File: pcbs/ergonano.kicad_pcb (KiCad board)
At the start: 2 copper layers, 171.6 x 164.6 mm, 87 parts

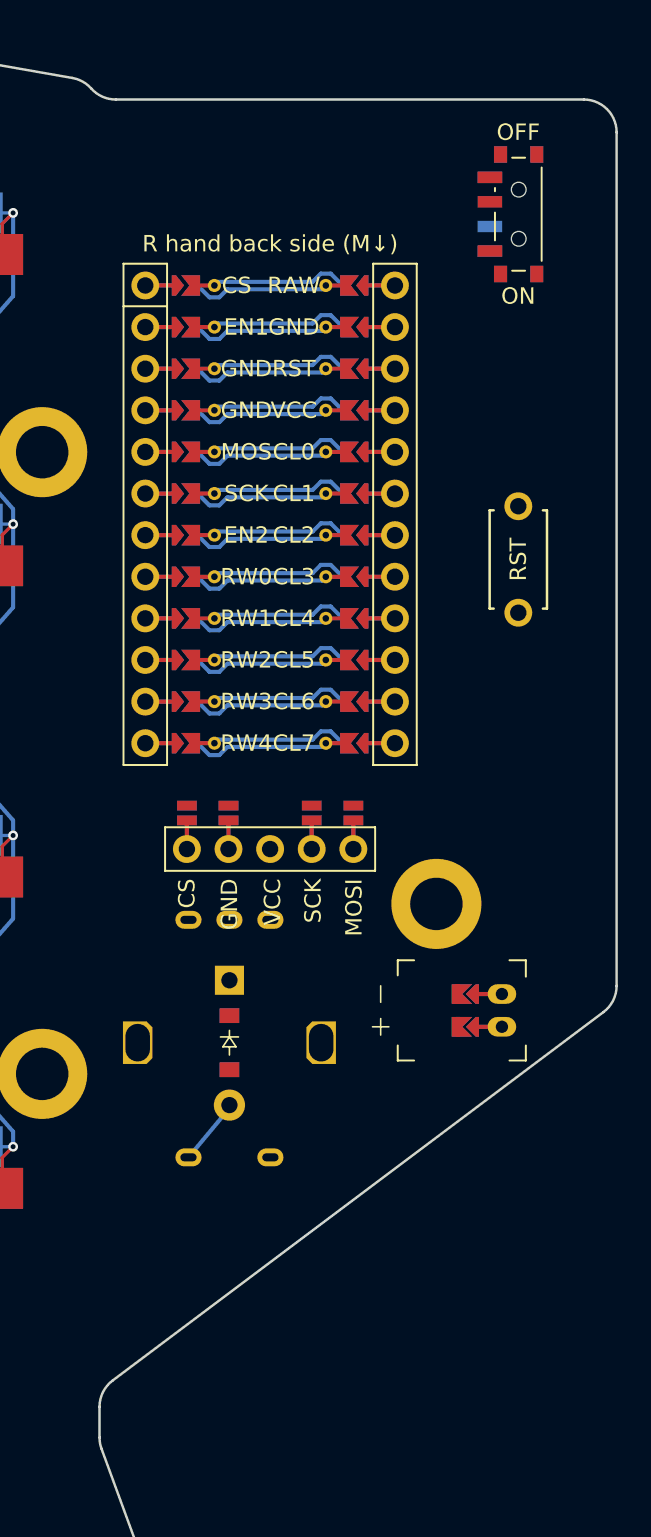
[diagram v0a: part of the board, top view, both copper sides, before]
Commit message: Tweaked layout, moved battery connector
shrinks the overall PCB by shrinking the mcu_padding
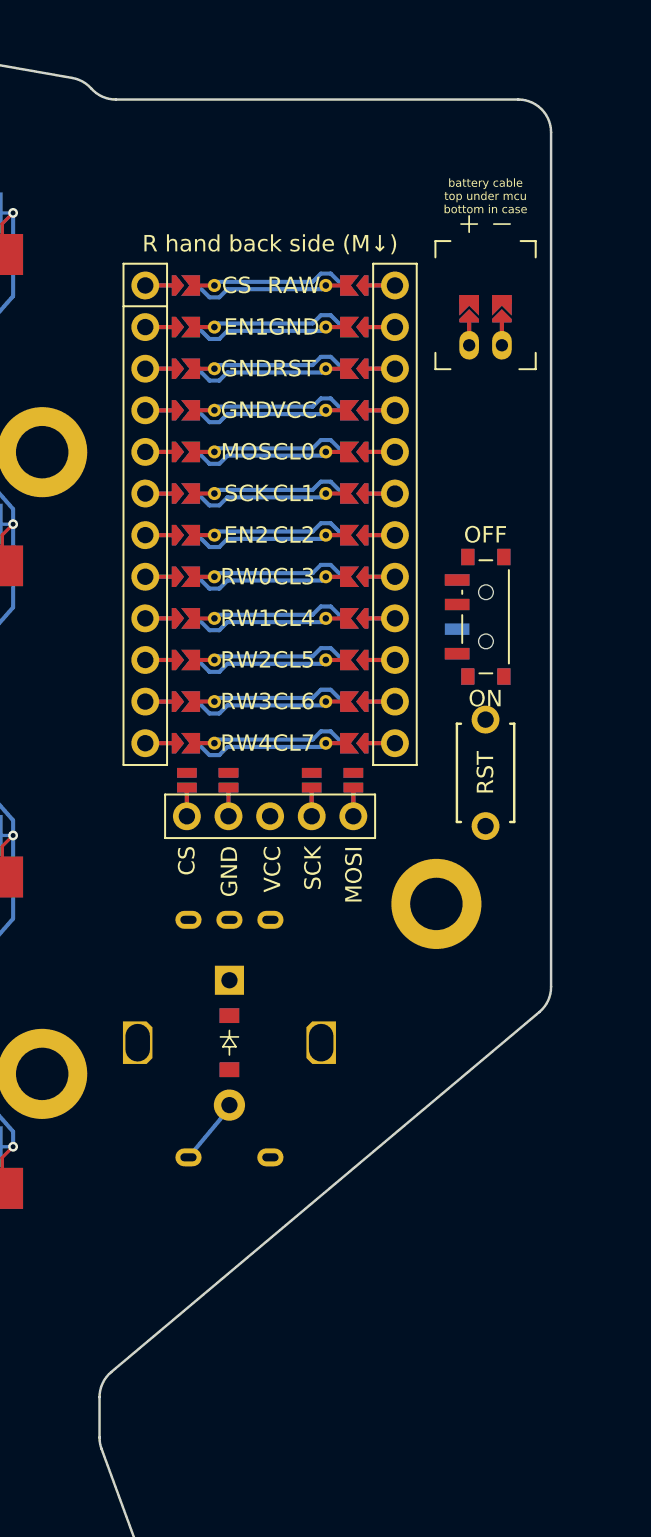
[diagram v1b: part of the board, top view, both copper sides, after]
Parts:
- moved JST1 40.6 mm to (200.6, 52.0), turned to 180 degrees
- moved PWR1 24.7 mm to (200.6, 68.6)
- moved RST1 13.2 mm to (200.6, 78.1)
- moved DISP1 2.00 mm to (187.4, 64.0)
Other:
- board size 171.6 x 164.6 mm -> 167.6 x 164.6 mm
- board text added: "battery cable top under mcu bottom in case"

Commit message: Use a drill for all screw holes on generated pcb plates
don't plate the encoder mounting holes (kicad jlcpcb violation)
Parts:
- added D35: , ceoloide:diode_tht_sod123, F.Cu at (139.2, 159.1)
- added D36: , ceoloide:diode_tht_sod123, F.Cu at (153.7, 146.9)
- added D37: , ceoloide:diode_tht_sod123, F.Cu at (151.4, 173.7)
- added D38: , ceoloide:diode_tht_sod123, F.Cu at (166.0, 161.5)
- added D39: , ceoloide:diode_tht_sod123, F.Cu at (185.0, 94.6)
- moved D34 67.0 mm to (134.2, 138.4), turned to 40 degrees
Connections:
- D34 pad 1: RW4 -> RW0
- D34 pad 2: encoder_encoder -> t_col0_near
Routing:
- net RW0: track 0.00 -> 34.6 mm
- net RW3: track 0.00 -> 34.6 mm
- net RW2: track 0.00 -> 34.6 mm
- net RW1: track 0.00 -> 34.6 mm
- net RW4: track 0.00 -> 25.9 mm
- net ring_num: track 13.8 -> 18.1 mm
- net middle_top: track 13.8 -> 18.1 mm
- net middle_num: track 13.8 -> 18.1 mm
- net index_num: track 13.8 -> 18.1 mm
- net pinky_num: track 13.8 -> 18.1 mm
- net outer_num: track 13.8 -> 18.1 mm
- net innermod_num: track 13.8 -> 18.1 mm
- net inner_num: track 13.8 -> 18.1 mm
- net ring_top: track 13.8 -> 18.1 mm
- net index_top: track 13.8 -> 18.1 mm
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
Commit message: moved the battery connector text
also resized to meet JLCPCB minimums
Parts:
- moved PWR1 9.52 mm to (200.6, 59.0)
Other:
- board text added: "mount battery connector top side if under mcu bottom side if larger"
- board text removed: "battery cable top under mcu bottom in case"
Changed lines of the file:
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@@
   (footprint "ceoloide:power_switch_smd_side"
     (layer "F.Cu")
-    (at 200.5875 68.57499999999999 0)
+    (at 200.5875 59.05 0)
     (property "Reference" "PWR1"
       (at -3.6 0 -90)
@@
     )
   )
-  (gr_text "battery cable\ntop under mcu\nbottom in case"
-    (at 200.5875 42.9 0)
-    (layer "F.SilkS" )
-    (effects
-      (font
-        (size 0.5 0.5)
-        (thickness 0.15)
-      )
-    )
-  )
-  (gr_text "battery cable\ntop under mcu\nbottom in case"
-    (at 200.5875 42.9 0)
-    (layer "B.SilkS" )
-    (effects
-      (font
-        (size 0.5 0.5)
-        (thickness 0.15)
-      )
+  (gr_text "mount battery connector\ntop side if under mcu\nbottom side if larger"
+    (at 187.4375 40 0)
+    (layer "F.SilkS" )
+    (effects
+      (font
+        (size 1 1)
+        (thickness 0.15)
+      )
+    )
+  )
+  (gr_text "mount battery connector\ntop side if under mcu\nbottom side if larger"
+    (at 187.4375 40 0)
+    (layer "B.SilkS" )
+    (effects
+      (font
+        (size 1 1)
+        (thickness 0.15)
+      )

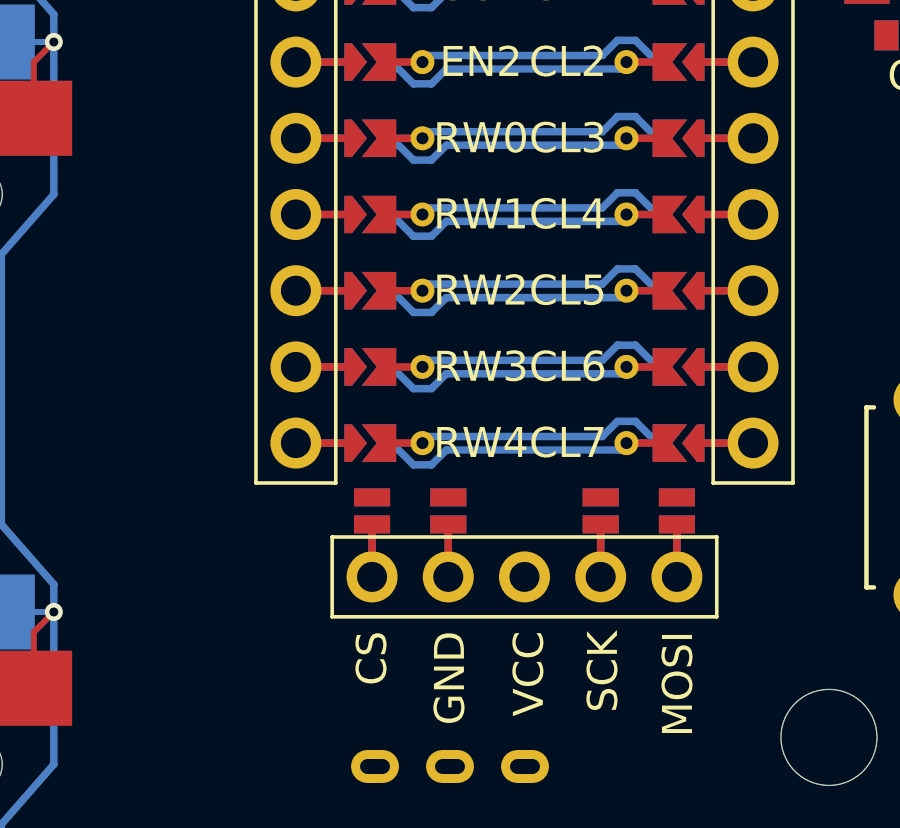
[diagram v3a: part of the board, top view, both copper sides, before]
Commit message: Small renames, tweaks to freerouting rules
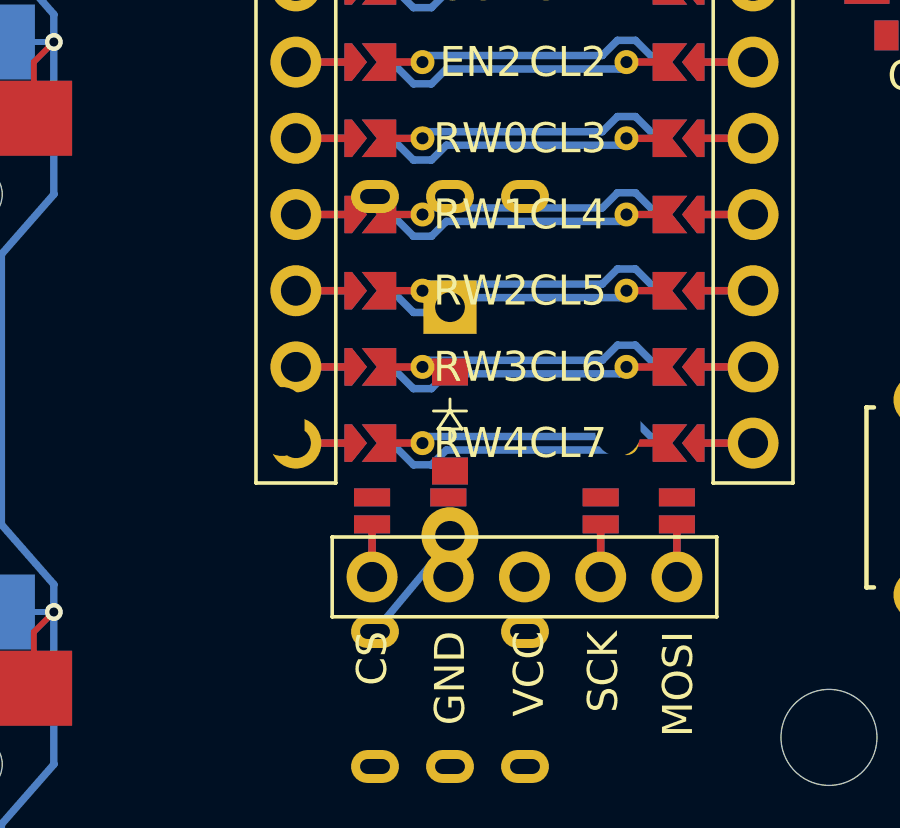
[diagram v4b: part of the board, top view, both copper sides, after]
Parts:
- added D40: , ceoloide:diode_tht_sod123, F.Cu at (185.0, 75.6)
- added RE2: , ceoloide:rotary_encoder_ec11_ec12, F.Cu at (185.0, 75.6)
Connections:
- net encoder_encoder renamed encoder_mcu
- D39 pad 1: RW4 -> (no net)
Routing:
- net (no net): track 918.1 -> 922.0 mm
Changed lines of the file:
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@@
   (title_block
     (title "ergonano")
-    (date "2026-10-30")
+    (date "2026-10-31")
     (rev "0.1")
     (company "aevumdecessus")
@@
 (net 96 "JST1_1")
 (net 97 "JST1_2")
-(net 98 "encoder_encoder")
+(net 98 "encoder_mcu")
+(net 99 "encoder_encoder")
   (footprint "ceoloide:switch_mx"
     (layer "B.Cu")
@@
     (pad "C" thru_hole oval (at -2.5 7.5 180) (size 1.6 1.1) (drill oval 1 0.5) (layers "*.Cu" "*.Mask") (net 62 "EN2"))
     (pad "S1" thru_hole oval (at -2.5 -7 180) (size 1.6 1.1) (drill oval 1 0.5) (layers "*.Cu" "*.Mask") (net 39 "CL6"))
-    (pad "S2" thru_hole oval (at 2.5 -7 180) (size 1.6 1.1) (drill oval 1 0.5) (layers "*.Cu" "*.Mask") (net 98 "encoder_encoder"))
+    (pad "S2" thru_hole oval (at 2.5 -7 180) (size 1.6 1.1) (drill oval 1 0.5) (layers "*.Cu" "*.Mask") (net 98 "encoder_mcu"))
+    (pad "" np_thru_hole oval
+      (at -5.6 0 90)
+      (size 2.3 1.5)
+      (drill oval 2.3 1.5)
+      (layers "*.Cu" "*.Mask")
+    )
+    (pad "" np_thru_hole oval
+      (at 5.6 0 90)
+      (size 2.3 1.5)
+      (drill oval 2.3 1.5)
+      (layers "*.Cu" "*.Mask")
+    )
+    (fp_rect (start -5.9 -6) (end 5.9 6) (layer "Dwgs.User") (stroke (width 0.15) (type solid)) (fill none))
+  )
+  (footprint "ceoloide:rotary_encoder_ec11_ec12"
+    (layer "F.Cu")
+    (at 184.95499999999998 75.57 180)
+    (property "Reference" "RE2"
+      (at 0 -8.5)
+      (layer "F.SilkS")
+      hide
+      (effects (font (size 1 1) (thickness 0.15)))
+    )
+    (attr through_hole)
+    (pad "A" thru_hole oval (at 2.5 7.5 180) (size 1.6 1.1) (drill oval 1 0.5) (layers "*.Cu" "*.Mask") (net 59 "EN1"))
+    (pad "B" thru_hole oval (at 0 7.5 180) (size 1.6 1.1) (drill oval 1 0.5) (layers "*.Cu" "*.Mask") (net 3 "GND"))
+    (pad "C" thru_hole oval (at -2.5 7.5 180) (size 1.6 1.1) (drill oval 1 0.5) (layers "*.Cu" "*.Mask") (net 62 "EN2"))
+    (pad "S1" thru_hole oval (at -2.5 -7 180) (size 1.6 1.1) (drill oval 1 0.5) (layers "*.Cu" "*.Mask") (net 39 "CL6"))
+    (pad "S2" thru_hole oval (at 2.5 -7 180) (size 1.6 1.1) (drill oval 1 0.5) (layers "*.Cu" "*.Mask") (net 99 "encoder_encoder"))
     (pad "" np_thru_hole oval
       (at -5.6 0 90)
@@
       (fp_line (start -0.35 0) (end -0.35 -0.55) (layer "F.SilkS") (stroke (width 0.1) (type solid)))
       (fp_line (start -0.75 0) (end -0.35 0) (layer "F.SilkS") (stroke (width 0.1) (type solid)))
+      (pad "1" smd rect (at -1.65 0 270) (size 0.9 1.2) (layers "F.Cu" "F.Paste" "F.Mask") (net 0 ""))
+      (pad "2" smd rect (at 1.65 0 270) (size 0.9 1.2) (layers "F.Cu" "F.Paste" "F.Mask") (net 98 "encoder_mcu"))
+      (fp_line (start 0.25 0) (end 0.75 0) (layer "B.SilkS") (stroke (width 0.1) (type solid)))
+      (fp_line (start 0.25 0.4) (end -0.35 0) (layer "B.SilkS") (stroke (width 0.1) (type solid)))
+      (fp_line (start 0.25 -0.4) (end 0.25 0.4) (layer "B.SilkS") (stroke (width 0.1) (type solid)))
+      (fp_line (start -0.35 0) (end 0.25 -0.4) (layer "B.SilkS") (stroke (width 0.1) (type solid)))
+      (fp_line (start -0.35 0) (end -0.35 0.55) (layer "B.SilkS") (stroke (width 0.1) (type solid)))
+      (fp_line (start -0.35 0) (end -0.35 -0.55) (layer "B.SilkS") (stroke (width 0.1) (type solid)))
+      (fp_line (start -0.75 0) (end -0.35 0) (layer "B.SilkS") (stroke (width 0.1) (type solid)))
+      (pad "1" smd rect (at -1.65 0 270) (size 0.9 1.2) (layers "B.Cu" "B.Paste" "B.Mask") (net 0 ""))
+      (pad "2" smd rect (at 1.65 0 270) (size 0.9 1.2) (layers "B.Cu" "B.Paste" "B.Mask") (net 98 "encoder_mcu"))
+      (pad "1" thru_hole rect (at -3.81 0 270) (size 1.778 1.778) (drill 0.9906) (layers "*.Cu" "*.Mask") (net 0 ""))
+      (pad "2" thru_hole circle (at 3.81 0 270) (size 1.905 1.905) (drill 0.9906) (layers "*.Cu" "*.Mask") (net 98 "encoder_mcu"))
+    )
+    (footprint "ceoloide:diode_tht_sod123"
+        (layer "F.Cu")
+        (at 184.95499999999998 75.57 270)
+        (property "Reference" "D40"
+            (at 0 0 270)
+            (layer "F.SilkS")
+            hide
+            (effects (font (size 1 1) (thickness 0.15)))
+        )
+      (fp_line (start 0.25 0) (end 0.75 0) (layer "F.SilkS") (stroke (width 0.1) (type solid)))
+      (fp_line (start 0.25 0.4) (end -0.35 0) (layer "F.SilkS") (stroke (width 0.1) (type solid)))
+      (fp_line (start 0.25 -0.4) (end 0.25 0.4) (layer "F.SilkS") (stroke (width 0.1) (type solid)))
+      (fp_line (start -0.35 0) (end 0.25 -0.4) (layer "F.SilkS") (stroke (width 0.1) (type solid)))
+      (fp_line (start -0.35 0) (end -0.35 0.55) (layer "F.SilkS") (stroke (width 0.1) (type solid)))
+      (fp_line (start -0.35 0) (end -0.35 -0.55) (layer "F.SilkS") (stroke (width 0.1) (type solid)))
+      (fp_line (start -0.75 0) (end -0.35 0) (layer "F.SilkS") (stroke (width 0.1) (type solid)))
       (pad "1" smd rect (at -1.65 0 270) (size 0.9 1.2) (layers "F.Cu" "F.Paste" "F.Mask") (net 50 "RW4"))
-      (pad "2" smd rect (at 1.65 0 270) (size 0.9 1.2) (layers "F.Cu" "F.Paste" "F.Mask") (net 98 "encoder_encoder"))
+      (pad "2" smd rect (at 1.65 0 270) (size 0.9 1.2) (layers "F.Cu" "F.Paste" "F.Mask") (net 99 "encoder_encoder"))
       (fp_line (start 0.25 0) (end 0.75 0) (layer "B.SilkS") (stroke (width 0.1) (type solid)))
       (fp_line (start 0.25 0.4) (end -0.35 0) (layer "B.SilkS") (stroke (width 0.1) (type solid)))
@@
       (fp_line (start -0.75 0) (end -0.35 0) (layer "B.SilkS") (stroke (width 0.1) (type solid)))
       (pad "1" smd rect (at -1.65 0 270) (size 0.9 1.2) (layers "B.Cu" "B.Paste" "B.Mask") (net 50 "RW4"))
-      (pad "2" smd rect (at 1.65 0 270) (size 0.9 1.2) (layers "B.Cu" "B.Paste" "B.Mask") (net 98 "encoder_encoder"))
+      (pad "2" smd rect (at 1.65 0 270) (size 0.9 1.2) (layers "B.Cu" "B.Paste" "B.Mask") (net 99 "encoder_encoder"))
       (pad "1" thru_hole rect (at -3.81 0 270) (size 1.778 1.778) (drill 0.9906) (layers "*.Cu" "*.Mask") (net 50 "RW4"))
-      (pad "2" thru_hole circle (at 3.81 0 270) (size 1.905 1.905) (drill 0.9906) (layers "*.Cu" "*.Mask") (net 98 "encoder_encoder"))
+      (pad "2" thru_hole circle (at 3.81 0 270) (size 1.905 1.905) (drill 0.9906) (layers "*.Cu" "*.Mask") (net 99 "encoder_encoder"))
     )
   (segment
@@
     (width 0.25)
     (locked yes)
+    (layer B.Cu)
+    (net 0)
+  )
+  (segment
+    (start 182.45499999999998 82.57)
+    (end 184.95499999999998 79.57)
+    (width 0.25)
+    (locked yes)
